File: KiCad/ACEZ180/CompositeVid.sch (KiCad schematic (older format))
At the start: 36 parts, among them Q1 2N3904, Q4 2N3904, X1 CRYSTALHC49U-V 6.556MHz

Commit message: Add Extra IO to Z180 board.
Signed-off-by: John Bradley <flypie@rocketmail.com>
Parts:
- removed R111: 18, Resistor_THT:R_Axial_DIN0204_L3.6mm_D1.6mm_P1.90mm_Vertical, symbol Device:R
- added RV1: 100, Potentiometer_THT:3362H1103LF, symbol Device:R_POT_TRIM
- Z10, Z11, Z9: value 74HCT393 -> SN74AHCT393N
- Z102: value 74HCT04 -> SN74AHCT04N
- Z19: value 74HCT00 -> SN74AHCT00N
- Z20: value 74HCT08 -> SN74AHCT08N
- Z21, Z22: value 74HCT11 -> SN74AHCT11N
- Z23: value 74HCT86 -> SN74AHCT86N
- Z25: value 74HCT02 -> SN74AHCT02N
- Z27: value 74HCT74 -> SN74AHCT74N
- Z28: renamed from Z12; value 74HCT166 -> SN74AHCT166N
- Z301: renamed from Z20; value 74HCT08 -> SN74AHCT08N
- renumbered C5 to C4, D100 to D10, D10 to D11, Q4 to Q2, R3 to R11, R107 to R12, R106 to R13, R102 to R14, R103 to R15, R4 to R16, R110 to R17, R9 to R3, R105 to R4, R104 to R7, R100 to R8, R101 to R9
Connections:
- net at COMPOSITE-OUT1.1 (Pin_1): now also RV1.2
- net at Q2.1 (E), R17.1: now also RV1.1
- no-connect marks 8 -> 9
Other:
- moved on the sheet: COMPOSITE-OUT1

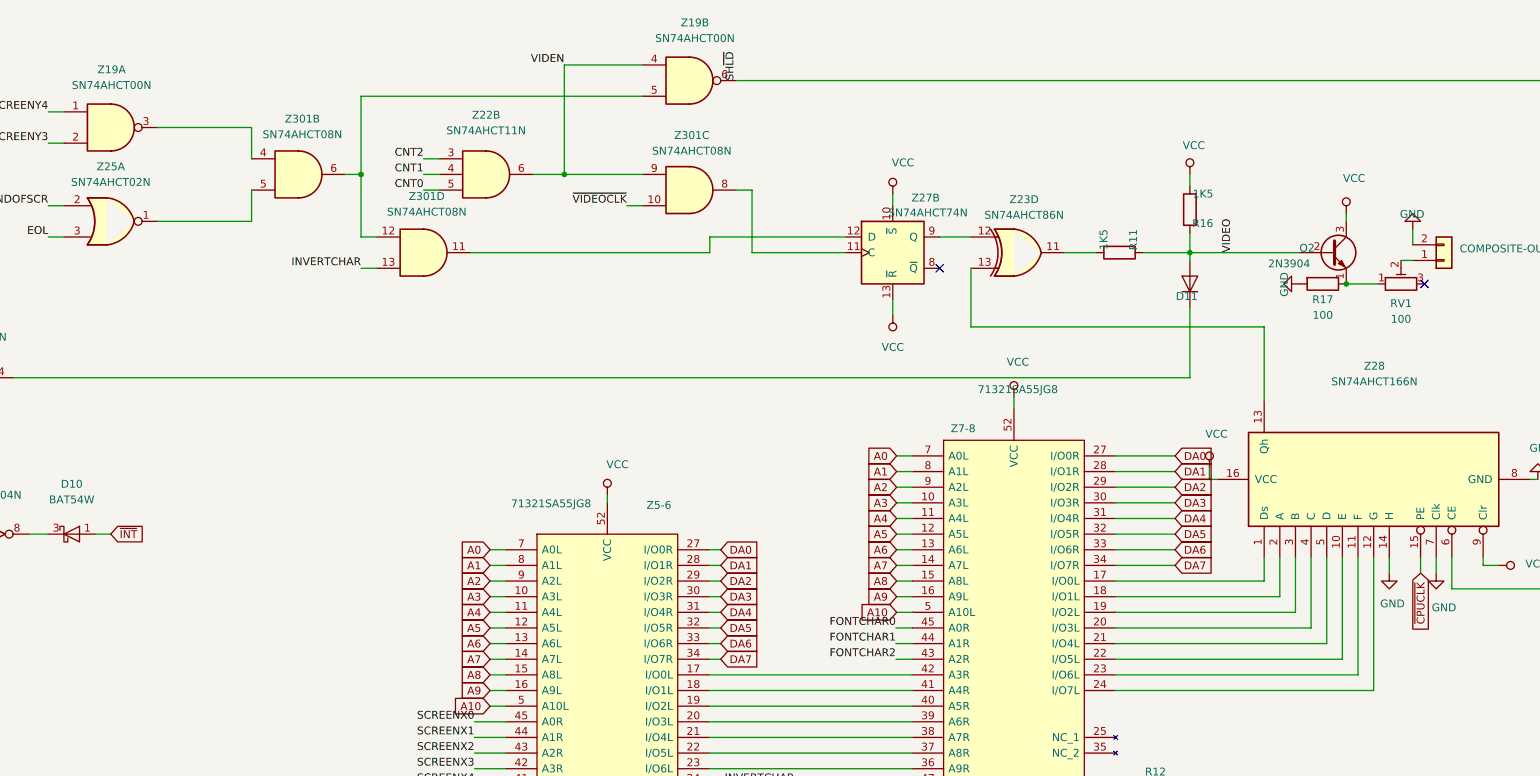
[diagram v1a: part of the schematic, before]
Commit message: Move Towards Ac3 test board, include KIO chip, regaranged port selection, ROM exapsion to 3000-3FFF relocated base of RAM to 4000 and inrease RAM to 48k. Change 40Hz interupt to work via CLK/TRG3 so the IM can be changed to use IM 2. This will require updated ROM.
Signed-off-by: John Bradley <flypie@rocketmail.com>
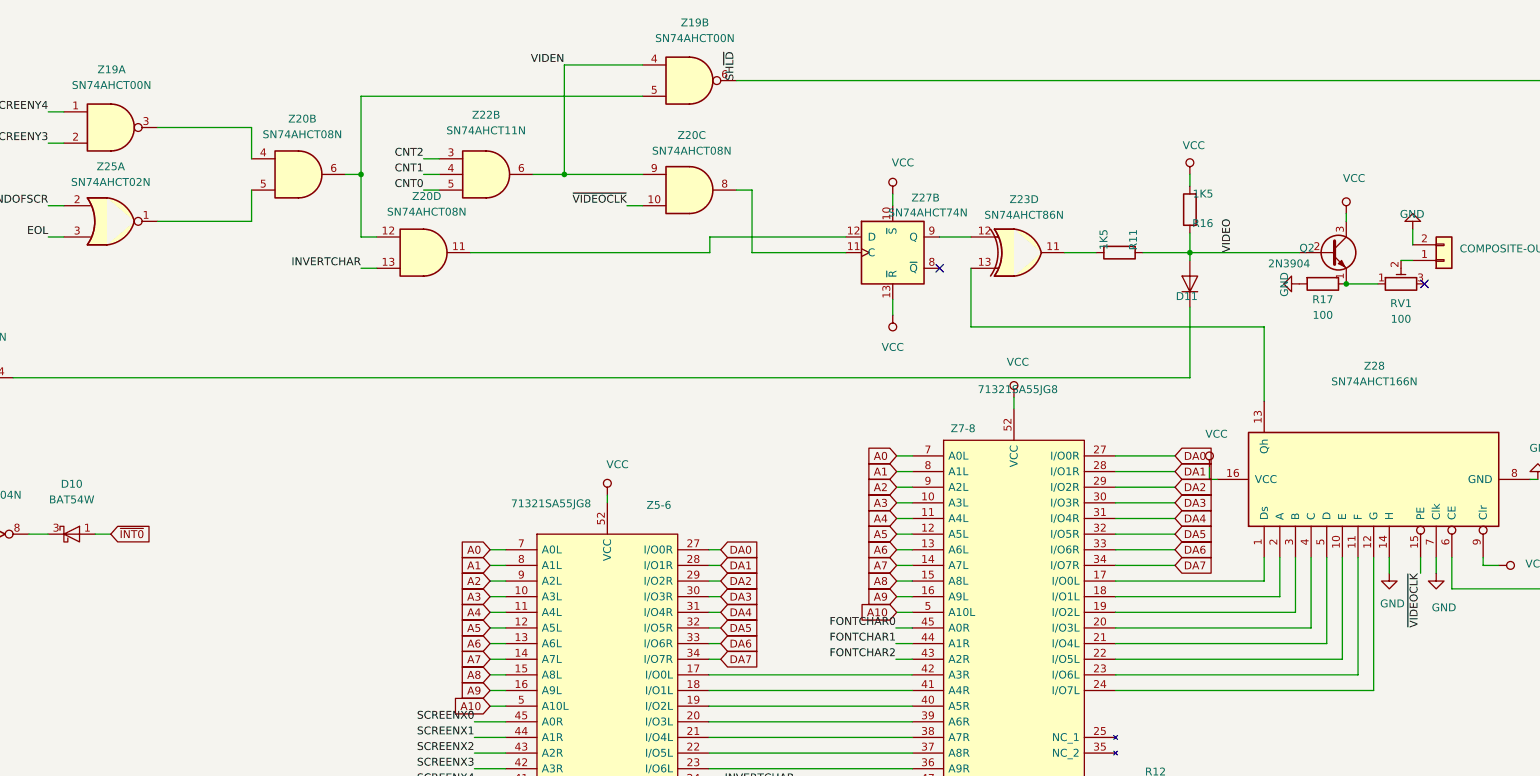
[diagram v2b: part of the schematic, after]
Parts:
- renumbered Z301 to Z20
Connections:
- net ~CPUCLK is gone; now on net ~VIDEOCLK: Z28.15 (PE)
- net ~INT renamed ~INT0
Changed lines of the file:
@@
 $EndComp
 $Comp
-L 74xx:74LS08 Z301
+L 74xx:74LS08 Z20
 U 2 1 5F80C874
 P 7850 2825
-F 0 "Z301" H 7875 3180 50  0000 C CNN
+F 0 "Z20" H 7875 3180 50  0000 C CNN
 F 1 "SN74AHCT08N" H 7875 3080 50  0000 C CNN
 F 2 "Package_DIP:DIP-14_W7.62mm" H 7850 2825 50  0001 C CNN
@@
 $EndComp
 $Comp
-L 74xx:74LS08 Z301
+L 74xx:74LS08 Z20
 U 4 1 5F80C880
 P 8650 3325
-F 0 "Z301" H 8670 3685 50  0000 C CNN
+F 0 "Z20" H 8670 3685 50  0000 C CNN
 F 1 "SN74AHCT08N" H 8670 3585 50  0000 C CNN
 F 2 "Package_DIP:DIP-14_W7.62mm" H 8650 3325 50  0001 C CNN
@@
 Wire Wire Line
 	13550 3325 14250 3325
-Text GLabel 15025 5375 3    50   Input ~ 0
-~CPUCLK
 Wire Wire Line
 	15525 5325 15425 5325
@@
 $EndComp
 $Comp
-L 74xx:74LS08 Z301
+L 74xx:74LS08 Z20
 U 3 1 5F80C87A
 P 10350 2925
-F 0 "Z301" H 10365 3275 50  0000 C CNN
+F 0 "Z20" H 10365 3275 50  0000 C CNN
 F 1 "SN74AHCT08N" H 10365 3175 50  0000 C CNN
 F 2 "Package_DIP:DIP-14_W7.62mm" H 10350 2925 50  0001 C CNN
@@
 Wire Wire Line
 	6550 5125 6650 5125
-Text GLabel 6650 5125 2    50   Input ~ 0
-~INT
 Text Label 730  1625 1    50   ~ 0
 ~VIDEOCLK
@@
 $EndComp
 NoConn ~ 15050 3525
+Text Label 15025 5375 3    50   ~ 0
+~VIDEOCLK
+Text GLabel 6650 5125 2    50   Input ~ 0
+~INT0
 $EndSCHEMATC

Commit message: Tidy up Capcitors in power supply to remove errors add labels.
Primary Development is now ACE3NOKB.


Signed-off-by: John Bradley <flypie@rocketmail.com>
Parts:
- removed R12, R13, R4, R7: R, Resistor_THT:R_Axial_DIN0204_L3.6mm_D1.6mm_P2.54mm_Vertical, symbol Device:R
- added R50, R51, R52, R53: 270, Resistor_THT:R_Axial_DIN0204_L3.6mm_D1.6mm_P2.54mm_Vertical, symbol Device:R
- C1, C4: footprint Capacitor_THT:C_Disc_D5.0mm_W2.5mm_P5.00mm -> Capacitor_THT:C_Disc_D3.0mm_W1.6mm_P2.50mm
- R14, R15, R8, R9: value R -> 270
- Z5-6, Z7-8: symbol SamacSys_Parts:71321SA55JG8 -> 7132la100pdg:IDT71321
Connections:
- net DA0: now also Z5-6.17 (I/O0L), Z7-8.17 (I/O0L); no longer Z5-6.27 (I/O0R), Z7-8.27 (I/O0R)
- net DA1: now also Z5-6.18 (I/O1L), Z7-8.18 (I/O1L); no longer Z5-6.28 (I/O1R), Z7-8.28 (I/O1R)
- net DA2: now also Z5-6.19 (I/O2L), Z7-8.19 (I/O2L); no longer Z5-6.29 (I/O2R), Z7-8.29 (I/O2R)
- net DA3: now also Z5-6.20 (I/O3L), Z7-8.20 (I/O3L); no longer Z5-6.30 (I/O3R), Z7-8.30 (I/O3R)
- net DA4: now also Z5-6.21 (I/O4L), Z7-8.21 (I/O4L); no longer Z5-6.31 (I/O4R), Z7-8.31 (I/O4R)
- net DA5: now also Z5-6.22 (I/O5L), Z7-8.22 (I/O5L); no longer Z5-6.32 (I/O5R), Z7-8.32 (I/O5R)
- net DA6: now also Z5-6.23 (I/O6L), Z7-8.23 (I/O6L); no longer Z5-6.33 (I/O6R), Z7-8.33 (I/O6R)
- net DA7: now also Z5-6.24 (I/O7L), Z7-8.24 (I/O7L); no longer Z5-6.34 (I/O7R), Z7-8.34 (I/O7R)
- net INVERTCHAR: now also Z5-6.34 (I/O7R); no longer Z5-6.24 (I/O7L)
- net VCC: now also R50.1, R51.1, R52.1, R53.1
- net at Z28.1 (Ds): now also Z7-8.27 (I/O0R); no longer Z7-8.17 (I/O0L)
- net at Z28.10 (E): now also Z7-8.32 (I/O5R); no longer Z7-8.22 (I/O5L)
- net at Z28.11 (F): now also Z7-8.33 (I/O6R); no longer Z7-8.23 (I/O6L)
- net at Z28.12 (G): now also Z7-8.34 (I/O7R); no longer Z7-8.24 (I/O7L)
- net at Z28.2 (A): now also Z7-8.28 (I/O1R); no longer Z7-8.18 (I/O1L)
- net at Z28.3 (B): now also Z7-8.29 (I/O2R); no longer Z7-8.19 (I/O2L)
- net at Z28.4 (C): now also Z7-8.30 (I/O3R); no longer Z7-8.20 (I/O3L)
- net at Z28.5 (D): now also Z7-8.31 (I/O4R); no longer Z7-8.21 (I/O4L)
- net at Z7-8.36 (A9R): now also Z5-6.33 (I/O6R); no longer Z5-6.23 (I/O6L)
- net at Z7-8.37 (A8R): now also Z5-6.32 (I/O5R); no longer Z5-6.22 (I/O5L)
- net at Z7-8.38 (A7R): now also Z5-6.31 (I/O4R); no longer Z5-6.21 (I/O4L)
- net at Z7-8.39 (A6R): now also Z5-6.30 (I/O3R); no longer Z5-6.20 (I/O3L)
- net at Z7-8.4 (~INTL): now also R52.2
- net at Z7-8.40 (A5R): now also Z5-6.29 (I/O2R); no longer Z5-6.19 (I/O2L)
- net at Z7-8.41 (A4R): now also Z5-6.28 (I/O1R); no longer Z5-6.18 (I/O1L)
- net at Z7-8.42 (A3R): now also Z5-6.27 (I/O0R); no longer Z5-6.17 (I/O0L)
- net at Z7-8.48 (~INTR): now also R53.2
- net at Z5-6.4 (~INTL): now also R50.2
- net at Z5-6.48 (~INTR): now also R51.2
- no-connect marks 9 -> 8
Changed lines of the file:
@@
 EESchema Schematic File Version 4
-LIBS:acez180-cache
-EELAYER 29 0
+EELAYER 30 0
 EELAYER END
 $Descr A3 16535 11693
@@
 Comment4 "This work is licensed under a Creative Commons "
 $EndDescr
-NoConn ~ 8775 8600
 Text Label 8650 2925 2    50   ~ 0
 CNT0
@@
 	12425 4325 12425 4250
 Wire Wire Line
-	10475 7475 10550 7475
-Wire Wire Line
-	10475 7575 10550 7575
-$Comp
-L Device:R R4
-U 1 1 672DCDCC
-P 10700 7475
-F 0 "R4" V 10450 7475 50  0000 C CNN
-F 1 "R" V 10550 7475 50  0000 C CNN
-F 2 "Resistor_THT:R_Axial_DIN0204_L3.6mm_D1.6mm_P2.54mm_Vertical" V 10630 7475 50  0001 C CNN
-F 3 "~" H 10700 7475 50  0001 C CNN
-	1    10700 7475
-	0    1    1    0
-$EndComp
-Wire Wire Line
-	10850 7475 10850 7575
-Connection ~ 10850 7575
-$Comp
-L Device:R R7
-U 1 1 672DCDC6
-P 10700 7575
-F 0 "R7" V 10450 7575 50  0000 C CNN
-F 1 "R" V 10550 7575 50  0000 C CNN
-F 2 "Resistor_THT:R_Axial_DIN0204_L3.6mm_D1.6mm_P2.54mm_Vertical" V 10630 7575 50  0001 C CNN
-F 3 "~" H 10700 7575 50  0001 C CNN
-	1    10700 7575
-	0    1    1    0
-$EndComp
-Wire Wire Line
 	10475 7925 10550 7925
 Wire Wire Line
@@
 U 1 1 5F80C8E6
 P 13300 7425
-F 0 "R15" V 13050 7430 50  0000 C CNN
-F 1 "R" V 13150 7430 50  0000 C CNN
+F 0 "R15" V 13425 7425 50  0000 C CNN
+F 1 "270" V 13525 7425 50  0000 C CNN
 F 2 "Resistor_THT:R_Axial_DIN0204_L3.6mm_D1.6mm_P2.54mm_Vertical" V 13230 7425 50  0001 C CNN
 F 3 "~" H 13300 7425 50  0001 C CNN
 	1    13300 7425
-	0    1    1    0
-$EndComp
-Wire Wire Line
-	13150 6975 13075 6975
-Wire Wire Line
-	13075 6875 13150 6875
-Wire Wire Line
-	13450 6875 13450 6975
-Connection ~ 13450 6975
-$Comp
-L Device:R R13
-U 1 1 65A56985
-P 13300 6975
-F 0 "R13" V 13070 7005 50  0000 C CNN
-F 1 "R" V 13170 7005 50  0000 C CNN
-F 2 "Resistor_THT:R_Axial_DIN0204_L3.6mm_D1.6mm_P2.54mm_Vertical" V 13230 6975 50  0001 C CNN
-F 3 "~" H 13300 6975 50  0001 C CNN
-	1    13300 6975
-	0    1    1    0
-$EndComp
-$Comp
-L Device:R R12
-U 1 1 65A5697F
-P 13300 6875
-F 0 "R12" V 13070 6905 50  0000 C CNN
-F 1 "R" V 13170 6905 50  0000 C CNN
-F 2 "Resistor_THT:R_Axial_DIN0204_L3.6mm_D1.6mm_P2.54mm_Vertical" V 13230 6875 50  0001 C CNN
-F 3 "~" H 13300 6875 50  0001 C CNN
-	1    13300 6875
 	0    1    1    0
 $EndComp
@@
 U 2 1 5F80C856
 P 11650 3325
+AR Path="/5F80C856" Ref="Z27"  Part="2"
+AR Path="/5FA4DA0E/5F80C856" Ref="Z27"  Part="2"
 F 0 "Z27" H 11860 3675 50  0000 C CNN
 F 1 "SN74AHCT74N" H 11875 3580 50  0000 C CNN
@@
 	0    -1   -1   0
 $EndComp
-Wire Wire Line
-	10850 7575 10850 7925
-Connection ~ 10850 7925
 $Comp
 L Device:R R8
 U 1 1 5F80C8DA
 P 10700 7925
-F 0 "R8" V 10450 7925 50  0000 C CNN
-F 1 "R" V 10550 7925 50  0000 C CNN
+F 0 "R8" V 10475 7925 50  0000 C CNN
+F 1 "270" V 10575 7925 50  0000 C CNN
 F 2 "Resistor_THT:R_Axial_DIN0204_L3.6mm_D1.6mm_P2.54mm_Vertical" V 10630 7925 50  0001 C CNN
 F 3 "~" H 10700 7925 50  0001 C CNN
@@
 U 1 1 5F80C8E0
 P 10700 8025
-F 0 "R9" V 10450 8025 50  0000 C CNN
-F 1 "R" V 10550 8025 50  0000 C CNN
+F 0 "R9" V 10825 8025 50  0000 C CNN
+F 1 "270" V 10925 8025 50  0000 C CNN
 F 2 "Resistor_THT:R_Axial_DIN0204_L3.6mm_D1.6mm_P2.54mm_Vertical" V 10630 8025 50  0001 C CNN
 F 3 "~" H 10700 8025 50  0001 C CNN
@@
 Wire Wire Line
 	13450 7325 13450 7425
-Wire Wire Line
-	13450 6975 13450 7325
-Connection ~ 13450 7325
 $Comp
 L Device:R R14
 U 1 1 5F80C8EC
 P 13300 7325
-F 0 "R14" V 13050 7330 50  0000 C CNN
-F 1 "R" V 13150 7330 50  0000 C CNN
+F 0 "R14" V 13075 7325 50  0000 C CNN
+F 1 "270" V 13175 7325 50  0000 C CNN
 F 2 "Resistor_THT:R_Axial_DIN0204_L3.6mm_D1.6mm_P2.54mm_Vertical" V 13230 7325 50  0001 C CNN
 F 3 "~" H 13300 7325 50  0001 C CNN
@@
 $EndComp
 $Comp
-L SamacSys_Parts:71321SA55JG8 Z7-8
+L 7132la100pdg:IDT71321 Z7-8
 U 1 1 5F80C938
 P 11775 4625
+AR Path="/5F80C938" Ref="Z7-8"  Part="1"
+AR Path="/5FA4DA0E/5F80C938" Ref="Z7-8"  Part="1"
 F 0 "Z7-8" H 12100 4800 50  0000 C CNN
 F 1 "71321SA55JG8" H 12450 5050 50  0000 C CNN
@@
 $EndComp
 $Comp
-L SamacSys_Parts:71321SA55JG8 Z5-6
+L 7132la100pdg:IDT71321 Z5-6
 U 1 1 5F80C942
 P 9175 5225
+AR Path="/5F80C942" Ref="Z5-6"  Part="1"
+AR Path="/5FA4DA0E/5F80C942" Ref="Z5-6"  Part="1"
 F 0 "Z5-6" H 10155 5510 50  0000 C CNN
 F 1 "71321SA55JG8" H 9465 5520 50  0000 C CNN
@@
 F 0 "C1" H 4800 8935 50  0000 L CNN
 F 1 "47nF" H 4800 8835 50  0000 L CNN
-F 2 "Capacitor_THT:C_Disc_D5.0mm_W2.5mm_P5.00mm" H 4700 8880 50  0001 C CNN
+F 2 "Capacitor_THT:C_Disc_D3.0mm_W1.6mm_P2.50mm" H 4700 8880 50  0001 C CNN
 F 3 "~" H 4700 8880 50  0001 C CNN
 	1    4700 8880
@@
 F 0 "C4" V 5005 8220 50  0000 C CNN
 F 1 "47nF" V 5105 8220 50  0000 C CNN
-F 2 "Capacitor_THT:C_Disc_D5.0mm_W2.5mm_P5.00mm" H 5255 8175 50  0001 C CNN
+F 2 "Capacitor_THT:C_Disc_D3.0mm_W1.6mm_P2.50mm" H 5255 8175 50  0001 C CNN
 F 3 "~" H 5255 8175 50  0001 C CNN
 	1    5255 8175
@@
 Text GLabel 6650 5125 2    50   Input ~ 0
 ~INT0
+$Comp
+L Device:R R50
+U 1 1 5DEEED88
+P 10700 7525
+F 0 "R50" V 10475 7525 50  0000 C CNN
+F 1 "270" V 10575 7525 50  0000 C CNN
+F 2 "Resistor_THT:R_Axial_DIN0204_L3.6mm_D1.6mm_P2.54mm_Vertical" V 10630 7525 50  0001 C CNN
+F 3 "~" H 10700 7525 50  0001 C CNN
+	1    10700 7525
+	0    1    1    0
+$EndComp
+Wire Wire Line
+	10850 7525 10850 7625
+Connection ~ 10850 7625
+$Comp
+L Device:R R51
+U 1 1 5DEEED91
+P 10700 7625
+F 0 "R51" V 10475 7625 50  0000 C CNN
+F 1 "270" V 10575 7625 50  0000 C CNN
+F 2 "Resistor_THT:R_Axial_DIN0204_L3.6mm_D1.6mm_P2.54mm_Vertical" V 10630 7625 50  0001 C CNN
+F 3 "~" H 10700 7625 50  0001 C CNN
+	1    10700 7625
+	0    1    1    0
+$EndComp
+Wire Wire Line
+	10850 7625 10850 7925
+Connection ~ 10850 7925
+Wire Wire Line
+	10375 7625 10550 7625
+Wire Wire Line
+	10375 7525 10550 7525
+$Comp
+L Device:R R52
+U 1 1 5DF62BE4
+P 13300 6925
+F 0 "R52" V 13075 6925 50  0000 C CNN
+F 1 "270" V 13175 6925 50  0000 C CNN
+F 2 "Resistor_THT:R_Axial_DIN0204_L3.6mm_D1.6mm_P2.54mm_Vertical" V 13230 6925 50  0001 C CNN
+F 3 "~" H 13300 6925 50  0001 C CNN
+	1    13300 6925
+	0    1    1    0
+$EndComp
+Wire Wire Line
+	13450 6925 13450 7025
+Connection ~ 13450 7025
+$Comp
+L Device:R R53
+U 1 1 5DF62BEC
+P 13300 7025
+F 0 "R53" V 13075 7025 50  0000 C CNN
+F 1 "270" V 13175 7025 50  0000 C CNN
+F 2 "Resistor_THT:R_Axial_DIN0204_L3.6mm_D1.6mm_P2.54mm_Vertical" V 13230 7025 50  0001 C CNN
+F 3 "~" H 13300 7025 50  0001 C CNN
+	1    13300 7025
+	0    1    1    0
+$EndComp
+Wire Wire Line
+	13450 7025 13450 7325
+Wire Wire Line
+	12975 7025 13150 7025
+Wire Wire Line
+	12975 6925 13150 6925
 $EndSCHEMATC

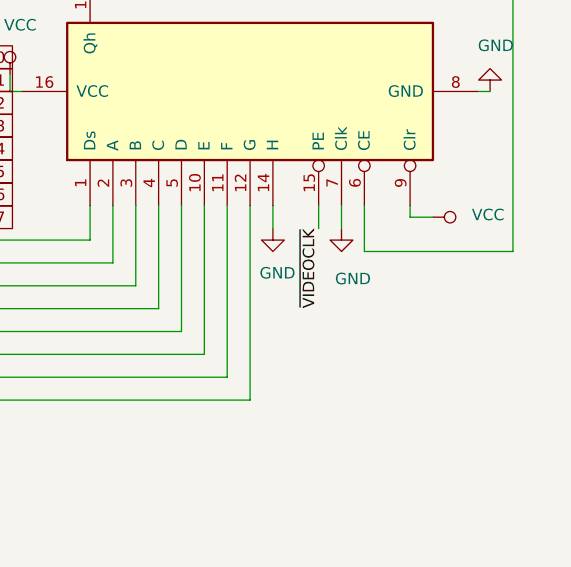
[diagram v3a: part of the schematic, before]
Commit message: Fix mistake on 74ALS166 Z28 connection clock connected to wrong pin. Add KeyBoard Project. Adjust resitor physical size.
Signed-off-by: John Bradley <flypie@rocketmail.com>
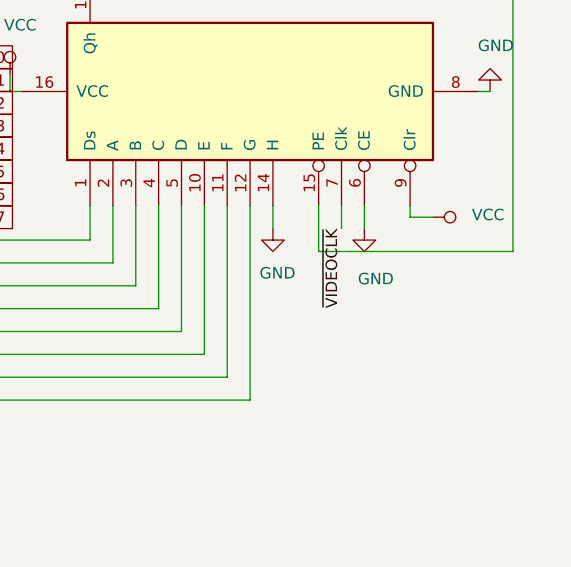
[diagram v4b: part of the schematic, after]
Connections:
- net GND: now also Z28.6 (CE); no longer Z28.7 (Clk)
- net SH~LD: now also Z28.15 (PE); no longer Z28.6 (CE)
- net ~VIDEOCLK: now also Z28.7 (Clk); no longer Z28.15 (PE)
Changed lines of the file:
@@
 EESchema Schematic File Version 4
+LIBS:acez180-cache
 EELAYER 30 0
 EELAYER END
@@
 $EndComp
 Wire Wire Line
+	15225 5275 15225 5375
+Wire Wire Line
+	14825 5275 14825 5375
+Wire Wire Line
+	15025 5275 15025 5475
+Wire Wire Line
 	15125 5275 15125 5375
-Wire Wire Line
-	14825 5275 14825 5375
-Wire Wire Line
-	15225 5275 15225 5475
-Wire Wire Line
-	15025 5275 15025 5375
 Wire Wire Line
 	14025 5275 14025 5425
@@
 L power:GND #0106
 U 1 1 5F80C593
-P 15125 5375
-F 0 "#0106" H 15125 5125 50  0001 C CNN
-F 1 "GND" H 15175 5155 50  0000 C CNN
-F 2 "" H 15125 5375 50  0001 C CNN
-F 3 "" H 15125 5375 50  0001 C CNN
-	1    15125 5375
+P 15225 5375
+F 0 "#0106" H 15225 5125 50  0001 C CNN
+F 1 "GND" H 15275 5155 50  0000 C CNN
+F 2 "" H 15225 5375 50  0001 C CNN
+F 3 "" H 15225 5375 50  0001 C CNN
+	1    15225 5375
 	1    0    0    -1
 $EndComp
@@
 Wire Wire Line
 	15875 5475 15875 2225
-Wire Wire Line
-	15225 5475 15875 5475
 Text Label 6475 8575 0    50   ~ 0
 ~VIDEOCLK
@@
 $EndComp
 NoConn ~ 15050 3525
-Text Label 15025 5375 3    50   ~ 0
+Text Label 15125 5375 3    50   ~ 0
 ~VIDEOCLK
 Text GLabel 6650 5125 2    50   Input ~ 0
@@
 Wire Wire Line
 	12975 6925 13150 6925
+Wire Wire Line
+	15025 5475 15875 5475
 $EndSCHEMATC
